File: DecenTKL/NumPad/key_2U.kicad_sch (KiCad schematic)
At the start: 4 parts, among them SW10 MX

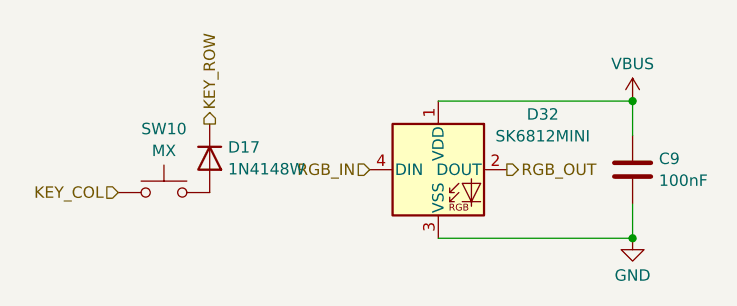
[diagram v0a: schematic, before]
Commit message: DecenTKL NumPad rev. 1 finalized
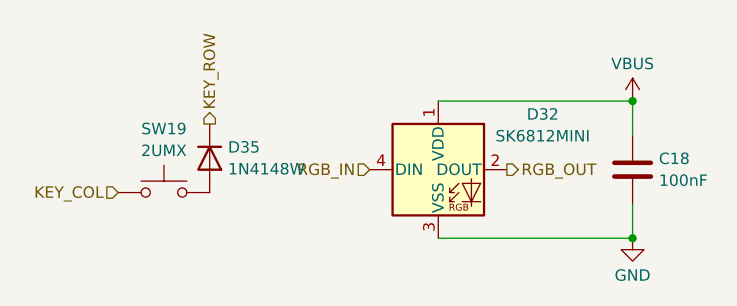
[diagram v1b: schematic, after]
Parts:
- SW19: renamed from SW10; value MX -> 2UMX; footprint DecenTKL:Kailh_socket_MX_1-00U -> DecenTKL:Kailh_socket_MX_2-00U
- renumbered C9 to C18, D17 to D35
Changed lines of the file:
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@@
 		(dnp no)
 		(fields_autoplaced yes)
-		(property "Reference" "D17"
+		(property "Reference" "D35"
 			(at 134.112 92.7678 90)
 			(effects
@@
 		(instances
 			(project "DecentNumPad"
-				(path "/2c073ed7-8422-482e-9fe5-a73c0717c131/3cb17e06-ad04-4d50-9565-8a9ba4ebdba3"
-					(reference "D17")
-					(unit 1)
-				)
-				(path "/2c073ed7-8422-482e-9fe5-a73c0717c131/3cc9818f-a1dd-49a1-a797-eead680f9c13"
-					(reference "D9")
-					(unit 1)
-				)
-				(path "/2c073ed7-8422-482e-9fe5-a73c0717c131/47263e08-18bb-4baa-bfdc-fd2b73c55f2c"
-					(reference "D19")
-					(unit 1)
-				)
-				(path "/2c073ed7-8422-482e-9fe5-a73c0717c131/50e112f8-7db7-4509-8296-ed8f130c3b51"
-					(reference "D23")
-					(unit 1)
-				)
-				(path "/2c073ed7-8422-482e-9fe5-a73c0717c131/5e50d4f3-eef1-4e8a-b10b-a2ad6b689406"
-					(reference "D11")
-					(unit 1)
-				)
-				(path "/2c073ed7-8422-482e-9fe5-a73c0717c131/8ad9e23f-c013-482d-8b93-6b9c6e6b27e1"
-					(reference "D21")
-					(unit 1)
-				)
-				(path "/2c073ed7-8422-482e-9fe5-a73c0717c131/8dd4f9a9-bc7c-4230-be17-825ff531f36d"
-					(reference "D5")
-					(unit 1)
-				)
-				(path "/2c073ed7-8422-482e-9fe5-a73c0717c131/928c8ada-72cc-4e10-8ca5-ddd099677834"
-					(reference "D27")
-					(unit 1)
-				)
-				(path "/2c073ed7-8422-482e-9fe5-a73c0717c131/cadcb80c-ec17-4247-82a6-215f9a6caa08"
-					(reference "D37")
-					(unit 1)
-				)
-				(path "/2c073ed7-8422-482e-9fe5-a73c0717c131/d3d1d945-161b-405a-bf56-811636d5130f"
-					(reference "D7")
-					(unit 1)
-				)
-				(path "/2c073ed7-8422-482e-9fe5-a73c0717c131/d6cd3d3d-b01a-48c9-bc9d-cdd0d81339fe"
-					(reference "D33")
-					(unit 1)
-				)
-				(path "/2c073ed7-8422-482e-9fe5-a73c0717c131/d8d7c9d6-0d55-4f8c-8727-e74c7394d356"
-					(reference "D29")
-					(unit 1)
-				)
-				(path "/2c073ed7-8422-482e-9fe5-a73c0717c131/e9257e38-6586-415d-baf8-64aa60d6b392"
-					(reference "D15")
-					(unit 1)
-				)
-				(path "/2c073ed7-8422-482e-9fe5-a73c0717c131/ee3ad1b0-d2dd-4554-bb3d-1ecbb9d48397"
-					(reference "D25")
+				(path "/2c073ed7-8422-482e-9fe5-a73c0717c131/7628d00f-9e3d-4cab-b942-743bdaf9e232"
+					(reference "D35")
 					(unit 1)
 				)
@@
 		(dnp no)
 		(fields_autoplaced yes)
-		(property "Reference" "#PWR083"
+		(property "Reference" "#PWR092"
 			(at 179.07 91.44 0)
 			(effects
@@
 		(instances
 			(project "DecentNumPad"
-				(path "/2c073ed7-8422-482e-9fe5-a73c0717c131/3cb17e06-ad04-4d50-9565-8a9ba4ebdba3"
-					(reference "#PWR083")
-					(unit 1)
-				)
-				(path "/2c073ed7-8422-482e-9fe5-a73c0717c131/3cc9818f-a1dd-49a1-a797-eead680f9c13"
-					(reference "#PWR079")
-					(unit 1)
-				)
-				(path "/2c073ed7-8422-482e-9fe5-a73c0717c131/47263e08-18bb-4baa-bfdc-fd2b73c55f2c"
-					(reference "#PWR084")
-					(unit 1)
-				)
-				(path "/2c073ed7-8422-482e-9fe5-a73c0717c131/50e112f8-7db7-4509-8296-ed8f130c3b51"
-					(reference "#PWR086")
-					(unit 1)
-				)
-				(path "/2c073ed7-8422-482e-9fe5-a73c0717c131/5e50d4f3-eef1-4e8a-b10b-a2ad6b689406"
-					(reference "#PWR080")
-					(unit 1)
-				)
-				(path "/2c073ed7-8422-482e-9fe5-a73c0717c131/8ad9e23f-c013-482d-8b93-6b9c6e6b27e1"
-					(reference "#PWR085")
-					(unit 1)
-				)
-				(path "/2c073ed7-8422-482e-9fe5-a73c0717c131/8dd4f9a9-bc7c-4230-be17-825ff531f36d"
-					(reference "#PWR077")
-					(unit 1)
-				)
-				(path "/2c073ed7-8422-482e-9fe5-a73c0717c131/928c8ada-72cc-4e10-8ca5-ddd099677834"
-					(reference "#PWR088")
-					(unit 1)
-				)
-				(path "/2c073ed7-8422-482e-9fe5-a73c0717c131/cadcb80c-ec17-4247-82a6-215f9a6caa08"
-					(reference "#PWR093")
-					(unit 1)
-				)
-				(path "/2c073ed7-8422-482e-9fe5-a73c0717c131/d3d1d945-161b-405a-bf56-811636d5130f"
-					(reference "#PWR078")
-					(unit 1)
-				)
-				(path "/2c073ed7-8422-482e-9fe5-a73c0717c131/d6cd3d3d-b01a-48c9-bc9d-cdd0d81339fe"
-					(reference "#PWR091")
-					(unit 1)
-				)
-				(path "/2c073ed7-8422-482e-9fe5-a73c0717c131/d8d7c9d6-0d55-4f8c-8727-e74c7394d356"
-					(reference "#PWR089")
-					(unit 1)
-				)
-				(path "/2c073ed7-8422-482e-9fe5-a73c0717c131/e9257e38-6586-415d-baf8-64aa60d6b392"
-					(reference "#PWR082")
-					(unit 1)
-				)
-				(path "/2c073ed7-8422-482e-9fe5-a73c0717c131/ee3ad1b0-d2dd-4554-bb3d-1ecbb9d48397"
-					(reference "#PWR087")
+				(path "/2c073ed7-8422-482e-9fe5-a73c0717c131/7628d00f-9e3d-4cab-b942-743bdaf9e232"
+					(reference "#PWR092")
 					(unit 1)
 				)
@@
 		(dnp no)
 		(fields_autoplaced yes)
-		(property "Reference" "C9"
+		(property "Reference" "C18"
 			(at 181.991 94.0378 0)
 			(effects
@@
 		(instances
 			(project "DecentNumPad"
-				(path "/2c073ed7-8422-482e-9fe5-a73c0717c131/3cb17e06-ad04-4d50-9565-8a9ba4ebdba3"
-					(reference "C9")
-					(unit 1)
-				)
-				(path "/2c073ed7-8422-482e-9fe5-a73c0717c131/3cc9818f-a1dd-49a1-a797-eead680f9c13"
-					(reference "C5")
-					(unit 1)
-				)
-				(path "/2c073ed7-8422-482e-9fe5-a73c0717c131/47263e08-18bb-4baa-bfdc-fd2b73c55f2c"
-					(reference "C10")
-					(unit 1)
-				)
-				(path "/2c073ed7-8422-482e-9fe5-a73c0717c131/50e112f8-7db7-4509-8296-ed8f130c3b51"
-					(reference "C12")
-					(unit 1)
-				)
-				(path "/2c073ed7-8422-482e-9fe5-a73c0717c131/5e50d4f3-eef1-4e8a-b10b-a2ad6b689406"
-					(reference "C6")
-					(unit 1)
-				)
-				(path "/2c073ed7-8422-482e-9fe5-a73c0717c131/8ad9e23f-c013-482d-8b93-6b9c6e6b27e1"
-					(reference "C11")
-					(unit 1)
-				)
-				(path "/2c073ed7-8422-482e-9fe5-a73c0717c131/8dd4f9a9-bc7c-4230-be17-825ff531f36d"
-					(reference "C3")
-					(unit 1)
-				)
-				(path "/2c073ed7-8422-482e-9fe5-a73c0717c131/928c8ada-72cc-4e10-8ca5-ddd099677834"
-					(reference "C14")
-					(unit 1)
-				)
-				(path "/2c073ed7-8422-482e-9fe5-a73c0717c131/cadcb80c-ec17-4247-82a6-215f9a6caa08"
-					(reference "C19")
-					(unit 1)
-				)
-				(path "/2c073ed7-8422-482e-9fe5-a73c0717c131/d3d1d945-161b-405a-bf56-811636d5130f"
-					(reference "C4")
-					(unit 1)
-				)
-				(path "/2c073ed7-8422-482e-9fe5-a73c0717c131/d6cd3d3d-b01a-48c9-bc9d-cdd0d81339fe"
-					(reference "C17")
-					(unit 1)
-				)
-				(path "/2c073ed7-8422-482e-9fe5-a73c0717c131/d8d7c9d6-0d55-4f8c-8727-e74c7394d356"
-					(reference "C15")
-					(unit 1)
-				)
-				(path "/2c073ed7-8422-482e-9fe5-a73c0717c131/e9257e38-6586-415d-baf8-64aa60d6b392"
-					(reference "C8")
-					(unit 1)
-				)
-				(path "/2c073ed7-8422-482e-9fe5-a73c0717c131/ee3ad1b0-d2dd-4554-bb3d-1ecbb9d48397"
-					(reference "C13")
+				(path "/2c073ed7-8422-482e-9fe5-a73c0717c131/7628d00f-9e3d-4cab-b942-743bdaf9e232"
+					(reference "C18")
 					(unit 1)
 				)
@@
 		(dnp no)
 		(fields_autoplaced yes)
-		(property "Reference" "SW10"
+		(property "Reference" "SW19"
 			(at 127 90.7245 0)
 			(effects
@@
 			)
 		)
-		(property "Value" "MX"
+		(property "Value" "2UMX"
 			(at 127 93.1488 0)
 			(effects
@@
 			)
 		)
-		(property "Footprint" "DecenTKL:Kailh_socket_MX_1-00U"
+		(property "Footprint" "DecenTKL:Kailh_socket_MX_2-00U"
 			(at 127 92.71 0)
 			(effects
@@
 		(instances
 			(project "DecentNumPad"
-				(path "/2c073ed7-8422-482e-9fe5-a73c0717c131/3cb17e06-ad04-4d50-9565-8a9ba4ebdba3"
-					(reference "SW10")
-					(unit 1)
-				)
-				(path "/2c073ed7-8422-482e-9fe5-a73c0717c131/3cc9818f-a1dd-49a1-a797-eead680f9c13"
-					(reference "SW6")
-					(unit 1)
-				)
-				(path "/2c073ed7-8422-482e-9fe5-a73c0717c131/47263e08-18bb-4baa-bfdc-fd2b73c55f2c"
-					(reference "SW11")
-					(unit 1)
-				)
-				(path "/2c073ed7-8422-482e-9fe5-a73c0717c131/50e112f8-7db7-4509-8296-ed8f130c3b51"
-					(reference "SW13")
-					(unit 1)
-				)
-				(path "/2c073ed7-8422-482e-9fe5-a73c0717c131/5e50d4f3-eef1-4e8a-b10b-a2ad6b689406"
-					(reference "SW7")
-					(unit 1)
-				)
-				(path "/2c073ed7-8422-482e-9fe5-a73c0717c131/8ad9e23f-c013-482d-8b93-6b9c6e6b27e1"
-					(reference "SW12")
-					(unit 1)
-				)
-				(path "/2c073ed7-8422-482e-9fe5-a73c0717c131/8dd4f9a9-bc7c-4230-be17-825ff531f36d"
-					(reference "SW4")
-					(unit 1)
-				)
-				(path "/2c073ed7-8422-482e-9fe5-a73c0717c131/928c8ada-72cc-4e10-8ca5-ddd099677834"
-					(reference "SW15")
-					(unit 1)
-				)
-				(path "/2c073ed7-8422-482e-9fe5-a73c0717c131/cadcb80c-ec17-4247-82a6-215f9a6caa08"
-					(reference "SW20")
-					(unit 1)
-				)
-				(path "/2c073ed7-8422-482e-9fe5-a73c0717c131/d3d1d945-161b-405a-bf56-811636d5130f"
-					(reference "SW5")
-					(unit 1)
-				)
-				(path "/2c073ed7-8422-482e-9fe5-a73c0717c131/d6cd3d3d-b01a-48c9-bc9d-cdd0d81339fe"
-					(reference "SW18")
-					(unit 1)
-				)
-				(path "/2c073ed7-8422-482e-9fe5-a73c0717c131/d8d7c9d6-0d55-4f8c-8727-e74c7394d356"
-					(reference "SW16")
-					(unit 1)
-				)
-				(path "/2c073ed7-8422-482e-9fe5-a73c0717c131/e9257e38-6586-415d-baf8-64aa60d6b392"
-					(reference "SW9")
-					(unit 1)
-				)
-				(path "/2c073ed7-8422-482e-9fe5-a73c0717c131/ee3ad1b0-d2dd-4554-bb3d-1ecbb9d48397"
-					(reference "SW14")
-					(unit 1)
-				)
+				(path "/2c073ed7-8422-482e-9fe5-a73c0717c131/7628d00f-9e3d-4cab-b942-743bdaf9e232"
+					(reference "SW19")
+					(unit 1)
+				)

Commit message: Fixed production orientation of one of the RGB LEDs
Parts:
- D32: JLCPCB Rotation Offset (none) -> 180
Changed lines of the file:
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@@
+			)
+		)
+		(property "JLCPCB Rotation Offset" "180"
+			(at 157.48 95.25 0)
+			(effects
+				(font
+					(size 1.27 1.27)
+				)
+				(hide yes)
 			)
 		)
